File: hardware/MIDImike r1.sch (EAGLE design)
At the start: 7 parts, among them SW1 PUSH-BTN

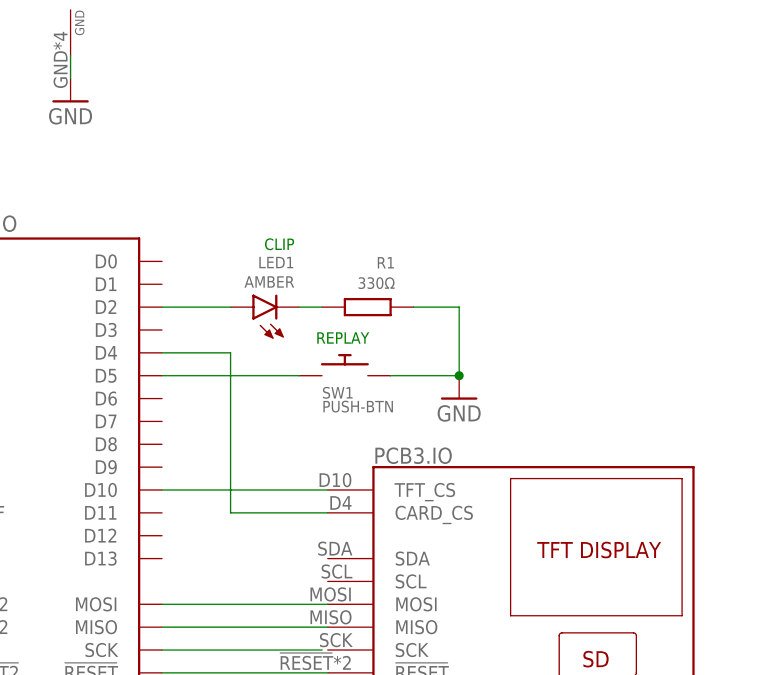
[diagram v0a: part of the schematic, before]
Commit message: add rotary dip switch to allow for pitch shift
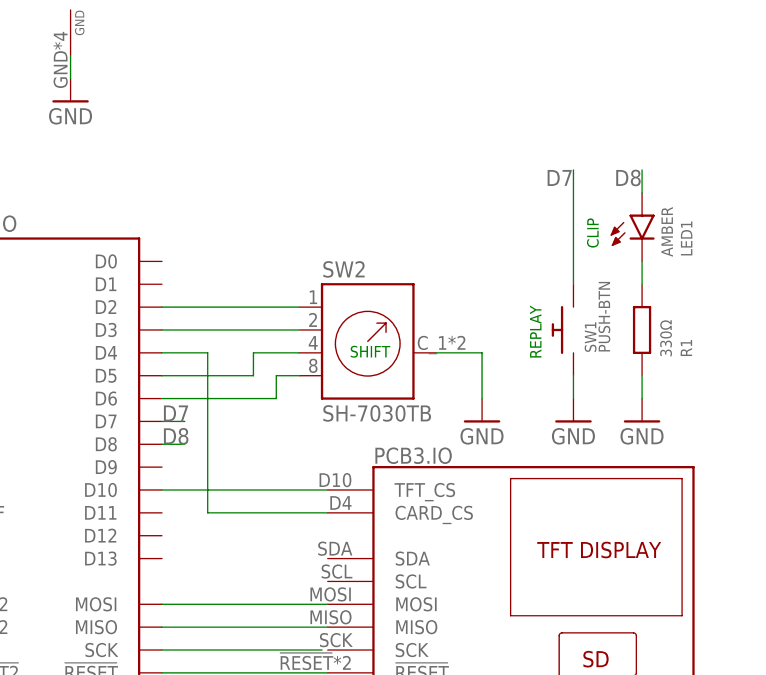
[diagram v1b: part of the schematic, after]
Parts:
- added SW2: SH-7030TB, Coert-Vonk:SH-7030TB
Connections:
- removed net REPLAY: PCB2.IO.D5, SW1.1
- new net D7: PCB2.IO.D7, SW1.2
- new net D8: LED1.A, PCB2.IO.D8
- new net N$10: PCB2.IO.D3, SW2.2
- new net N$13: PCB2.IO.D5, SW2.4
- new net N$14: PCB2.IO.D6, SW2.8
- net GND: now also SW1.1, SW2.C; no longer SW1.2
- net N$1: now also SW2.1; no longer LED1.A
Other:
- note added: "SHIFT"
- moved on the sheet: LED1, R1, SW1
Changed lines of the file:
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@@
 <part name="LED1" library="OPNpool" deviceset="LED" device="CHIPLED_0805" package3d_urn="urn:adsk.eagle:package:15821/2" value="AMBER"/>
 <part name="GND4" library="Coert-Vonk" deviceset="GND" device=""/>
+<part name="GND7" library="Coert-Vonk" deviceset="GND" device=""/>
+<part name="GND8" library="Coert-Vonk" deviceset="GND" device=""/>
+<part name="SW2" library="Coert-Vonk" deviceset="SH-7030TB" device=""/>
 </parts>
 <sheets>
@@
 <plain>
 <text x="40.64" y="88.9" size="1.778" layer="91" align="bottom-center">USB-MIDI</text>
-<text x="103.886" y="110.236" size="1.27" layer="91" align="bottom-center">REPLAY</text>
+<text x="125.984" y="111.506" size="1.27" layer="91" rot="R90" align="bottom-center">REPLAY</text>
 <text x="55.88" y="66.04" size="1.778" layer="91" align="bottom-right">USB-MIDI or USB-SERIAL</text>
-<text x="98.552" y="120.65" size="1.27" layer="91" align="bottom-right">CLIP</text>
+<text x="132.334" y="124.206" size="1.27" layer="91" rot="R90" align="bottom-right">CLIP</text>
+<text x="106.934" y="109.982" size="1.27" layer="91" rot="R180" align="bottom-center">SHIFT</text>
 </plain>
 <instances>
@@
 <attribute name="VALUE" x="60.96" y="134.62" size="1.778" layer="96" align="bottom-center"/>
 </instance>
-<instance part="SW1" gate="G$1" x="104.14" y="106.68" smashed="yes">
-<attribute name="NAME" x="101.598090625" y="104.14381875" size="1.27" layer="95"/>
-<attribute name="VALUE" x="101.598190625" y="102.612390625" size="1.27" layer="96"/>
+<instance part="SW1" gate="G$1" x="129.54" y="111.76" smashed="yes" rot="R90">
+<attribute name="NAME" x="132.07618125" y="109.218090625" size="1.27" layer="95" rot="R90"/>
+<attribute name="VALUE" x="133.607609375" y="109.218190625" size="1.27" layer="96" rot="R90"/>
 </instance>
 <instance part="GND5" gate="1" x="40.64" y="76.2" smashed="yes">
 <attribute name="VALUE" x="40.64" y="73.66" size="1.778" layer="96" align="bottom-center"/>
 </instance>
-<instance part="GND6" gate="1" x="116.84" y="104.14" smashed="yes">
-<attribute name="VALUE" x="116.84" y="101.6" size="1.778" layer="96" align="bottom-center"/>
+<instance part="GND6" gate="1" x="137.16" y="101.6" smashed="yes">
+<attribute name="VALUE" x="137.16" y="99.06" size="1.778" layer="96" align="bottom-center"/>
 </instance>
 <instance part="PCB1" gate=".IO" x="27.94" y="111.76" smashed="yes">
@@
 <attribute name="VALUE" x="46.355" y="83.82" size="1.778" layer="96" rot="R90"/>
 </instance>
-<instance part="R1" gate="G$1" x="106.68" y="114.3" smashed="yes" rot="MR0">
-<attribute name="MANF" x="106.68" y="114.3" size="1.778" layer="96" rot="MR0" display="off"/>
-<attribute name="MANF#" x="106.68" y="114.3" size="1.778" layer="96" rot="MR0" display="off"/>
-<attribute name="MOUSER#" x="106.68" y="114.3" size="1.778" layer="96" rot="MR0" display="off"/>
-<attribute name="NAME" x="109.728" y="118.5926" size="1.27" layer="95" rot="MR0"/>
-<attribute name="VALUE" x="109.728" y="116.332" size="1.27" layer="96" rot="MR0"/>
-</instance>
-<instance part="LED1" gate="G$1" x="93.98" y="114.3" smashed="yes" rot="R90">
-<attribute name="NAME" x="98.552" y="119.888" size="1.27" layer="95" rot="R180"/>
-<attribute name="VALUE" x="98.552" y="117.729" size="1.27" layer="96" rot="R180"/>
+<instance part="R1" gate="G$1" x="137.16" y="111.76" smashed="yes" rot="MR90">
+<attribute name="MANF" x="137.16" y="111.76" size="1.778" layer="96" rot="MR90" display="off"/>
+<attribute name="MANF#" x="137.16" y="111.76" size="1.778" layer="96" rot="MR90" display="off"/>
+<attribute name="MOUSER#" x="137.16" y="111.76" size="1.778" layer="96" rot="MR90" display="off"/>
+<attribute name="NAME" x="141.4526" y="108.712" size="1.27" layer="95" rot="MR90"/>
+<attribute name="VALUE" x="139.192" y="108.712" size="1.27" layer="96" rot="MR90"/>
+</instance>
+<instance part="LED1" gate="G$1" x="137.16" y="124.46" smashed="yes">
+<attribute name="NAME" x="142.748" y="119.888" size="1.27" layer="95" rot="R90"/>
+<attribute name="VALUE" x="140.589" y="119.888" size="1.27" layer="96" rot="R90"/>
 </instance>
 <instance part="GND4" gate="1" x="45.72" y="104.14" smashed="yes">
 <attribute name="VALUE" x="45.72" y="101.6" size="1.778" layer="96" align="bottom-center"/>
+</instance>
+<instance part="GND7" gate="1" x="129.54" y="101.6" smashed="yes">
+<attribute name="VALUE" x="129.54" y="99.06" size="1.778" layer="96" align="bottom-center"/>
+</instance>
+<instance part="GND8" gate="1" x="119.38" y="101.6" smashed="yes">
+<attribute name="VALUE" x="119.38" y="99.06" size="1.778" layer="96" align="bottom-center"/>
+</instance>
+<instance part="SW2" gate="G$1" x="106.68" y="109.22" smashed="yes">
+<attribute name="NAME" x="101.6" y="117.602" size="1.778" layer="95"/>
+<attribute name="VALUE" x="101.6" y="103.378" size="1.778" layer="96" align="top-left"/>
 </instance>
 </instances>
@@
 </segment>
 <segment>
-<pinref part="SW1" gate="G$1" pin="2"/>
-<wire x1="109.22" y1="106.68" x2="116.84" y2="106.68" width="0.1524" layer="91"/>
 <pinref part="GND6" gate="1" pin="GND"/>
-<wire x1="116.84" y1="114.3" x2="116.84" y2="106.68" width="0.1524" layer="91"/>
-<junction x="116.84" y="106.68"/>
 <pinref part="R1" gate="G$1" pin="1"/>
-<wire x1="111.76" y1="114.3" x2="116.84" y2="114.3" width="0.1524" layer="91"/>
+<wire x1="137.16" y1="106.68" x2="137.16" y2="104.14" width="0.1524" layer="91"/>
 </segment>
 <segment>
@@
 <wire x1="45.72" y1="116.84" x2="45.72" y2="106.68" width="0.1524" layer="91"/>
 </segment>
+<segment>
+<wire x1="129.54" y1="106.68" x2="129.54" y2="104.14" width="0.1524" layer="91"/>
+<pinref part="SW1" gate="G$1" pin="1"/>
+<pinref part="GND7" gate="1" pin="GND"/>
+</segment>
+<segment>
+<pinref part="SW2" gate="G$1" pin="C"/>
+<pinref part="GND8" gate="1" pin="GND"/>
+<wire x1="114.3" y1="109.22" x2="119.38" y2="109.22" width="0.1524" layer="91"/>
+<wire x1="119.38" y1="109.22" x2="119.38" y2="104.14" width="0.1524" layer="91"/>
+</segment>
 </net>
 <net name="5V" class="0">
@@
 <net name="N$9" class="0">
 <segment>
-<wire x1="83.82" y1="109.22" x2="91.44" y2="109.22" width="0.1524" layer="91"/>
+<wire x1="83.82" y1="109.22" x2="88.9" y2="109.22" width="0.1524" layer="91"/>
 <pinref part="PCB3" gate=".IO" pin="CARD_CS"/>
-<wire x1="91.44" y1="109.22" x2="91.44" y2="91.44" width="0.1524" layer="91"/>
-<wire x1="91.44" y1="91.44" x2="102.235" y2="91.44" width="0.1524" layer="91"/>
+<wire x1="88.9" y1="109.22" x2="88.9" y2="91.44" width="0.1524" layer="91"/>
+<wire x1="88.9" y1="91.44" x2="102.235" y2="91.44" width="0.1524" layer="91"/>
 <pinref part="PCB2" gate=".IO" pin="D4"/>
-</segment>
-</net>
-<net name="REPLAY" class="0">
-<segment>
-<wire x1="83.82" y1="106.68" x2="99.06" y2="106.68" width="0.1524" layer="91"/>
-<pinref part="SW1" gate="G$1" pin="1"/>
-<pinref part="PCB2" gate=".IO" pin="D5"/>
 </segment>
 </net>
@@
 </segment>
 </net>
-<net name="N$1" class="0">
-<segment>
-<pinref part="PCB2" gate=".IO" pin="D2"/>
-<pinref part="LED1" gate="G$1" pin="A"/>
-<wire x1="83.82" y1="114.3" x2="91.44" y2="114.3" width="0.1524" layer="91"/>
-</segment>
-</net>
 <net name="N$8" class="0">
 <segment>
 <pinref part="LED1" gate="G$1" pin="C"/>
 <pinref part="R1" gate="G$1" pin="2"/>
-<wire x1="99.06" y1="114.3" x2="101.6" y2="114.3" width="0.1524" layer="91"/>
-</segment>
-</net>
+<wire x1="137.16" y1="119.38" x2="137.16" y2="116.84" width="0.1524" layer="91"/>
+</segment>
+</net>
+<net name="D8" class="0">
+<segment>
+<pinref part="LED1" gate="G$1" pin="A"/>
+<wire x1="137.16" y1="127" x2="137.16" y2="129.54" width="0.1524" layer="91"/>
+<label x="137.16" y="129.54" size="1.778" layer="95" rot="R180"/>
+</segment>
+<segment>
+<pinref part="PCB2" gate=".IO" pin="D8"/>
+<wire x1="83.82" y1="99.06" x2="86.36" y2="99.06" width="0.1524" layer="91"/>
+<label x="83.82" y="99.06" size="1.778" layer="95"/>
+</segment>
+</net>
+<net name="N$13" class="0">
+<segment>
+<pinref part="PCB2" gate=".IO" pin="D5"/>
+<wire x1="83.82" y1="106.68" x2="93.98" y2="106.68" width="0.1524" layer="91"/>
+<wire x1="93.98" y1="106.68" x2="93.98" y2="109.22" width="0.1524" layer="91"/>
+<wire x1="93.98" y1="109.22" x2="99.06" y2="109.22" width="0.1524" layer="91"/>
+<pinref part="SW2" gate="G$1" pin="4"/>
+</segment>
+</net>
+<net name="N$14" class="0">
+<segment>
+<pinref part="PCB2" gate=".IO" pin="D6"/>
+<wire x1="83.82" y1="104.14" x2="96.52" y2="104.14" width="0.1524" layer="91"/>
+<wire x1="96.52" y1="104.14" x2="96.52" y2="106.68" width="0.1524" layer="91"/>
+<wire x1="96.52" y1="106.68" x2="99.06" y2="106.68" width="0.1524" layer="91"/>
+<pinref part="SW2" gate="G$1" pin="8"/>
+</segment>
+</net>
+<net name="D7" class="0">
+<segment>
+<pinref part="PCB2" gate=".IO" pin="D7"/>
+<wire x1="83.82" y1="101.6" x2="86.36" y2="101.6" width="0.1524" layer="91"/>
+<label x="83.82" y="101.6" size="1.778" layer="95"/>
+</segment>
+<segment>
+<pinref part="SW1" gate="G$1" pin="2"/>
+<wire x1="129.54" y1="116.84" x2="129.54" y2="129.54" width="0.1524" layer="91"/>
+<label x="129.54" y="129.54" size="1.778" layer="95" rot="R180"/>
+</segment>
+</net>
+<net name="N$1" class="0">
+<segment>
+<pinref part="PCB2" gate=".IO" pin="D2"/>
+<wire x1="83.82" y1="114.3" x2="99.06" y2="114.3" width="0.1524" layer="91"/>
+<pinref part="SW2" gate="G$1" pin="1"/>
+</segment>
+</net>
+<net name="N$10" class="0">
+<segment>
+<pinref part="PCB2" gate=".IO" pin="D3"/>
+<pinref part="SW2" gate="G$1" pin="2"/>
+<wire x1="83.82" y1="111.76" x2="99.06" y2="111.76" width="0.1524" layer="91"/>
+</segment>
+</net>
